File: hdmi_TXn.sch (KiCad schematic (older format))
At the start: 21 parts

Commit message: Fix issues due to different KiCad version
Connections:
- wire segments 106 -> 96
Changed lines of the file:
@@
 U 1 1 57C07751
 P 10600 4950
+AR Path="/57C07751" Ref="R$TXn$3"  Part="1"
+AR Path="/57C01383/57C07751" Ref="R$TXn$3"  Part="1"
 F 0 "R$TXn$3" V 10700 4950 50  0000 C CNN
 F 1 "R" V 10607 4951 50  0000 C CNN
@@
 U 1 1 57C07753
 P 3900 4400
+AR Path="/57C07753" Ref="R$TXn$1"  Part="1"
+AR Path="/57C01383/57C07753" Ref="R$TXn$1"  Part="1"
 F 0 "R$TXn$1" V 3800 4400 50  0000 C CNN
 F 1 "R" V 3907 4401 50  0000 C CNN
@@
 U 1 1 57C07755
 P 4000 4400
+AR Path="/57C07755" Ref="R$TXn$2"  Part="1"
+AR Path="/57C01383/57C07755" Ref="R$TXn$2"  Part="1"
 F 0 "R$TXn$2" V 4080 4400 50  0000 C CNN
 F 1 "R" V 4007 4401 50  0000 C CNN
@@
 	11750 4850 11600 4850
 Wire Wire Line
-	11600 4850 11600 5150
-Wire Wire Line
-	11600 5150 11600 5450
-Wire Wire Line
-	11600 5450 11600 5750
-Wire Wire Line
-	11600 5750 11600 6350
-Wire Wire Line
-	11600 6350 11600 6900
+	11600 4850 11600 6900
 Wire Wire Line
 	11750 5150 11600 5150
@@
 	6400 5800 6750 5800
 Wire Wire Line
-	8150 6600 8550 6600
-Wire Wire Line
-	8550 6600 9000 6600
+	8150 6600 9000 6600
 Wire Wire Line
 	8150 6400 9000 6400
 Wire Wire Line
-	7400 3750 7450 3750
-Wire Wire Line
-	7450 3750 7500 3750
+	7400 3750 7500 3750
 Wire Wire Line
 	7450 3750 7450 3600
@@
 Connection ~ 11600 6350
 Wire Wire Line
-	9800 5950 10600 5950
-Wire Wire Line
-	10600 5950 11750 5950
+	9800 5950 11750 5950
 Wire Wire Line
 	10600 5950 10600 5650
 Wire Wire Line
-	10600 5200 10600 5250
-Wire Wire Line
-	10600 4450 10600 4700
+	10600 5100 10600 5250
+Wire Wire Line
+	10600 4450 10600 4800
 Connection ~ 10600 5950
 Wire Wire Line
@@
 	5400 4800 6200 4800
 Wire Wire Line
-	4000 4100 4000 4150
+	4000 4100 4000 4250
 $Comp
 L VCC3V3 #PWR3
@@
 $EndComp
 Wire Wire Line
-	3900 4100 3950 4100
-Wire Wire Line
-	3950 4100 4000 4100
+	3900 4100 4000 4100
 Text Label 3800 5900 2    60   ~ 0
 HDMIP_$TXn$_SCL
@@
 U 1 1 57C07769
 P 3900 5600
+AR Path="/57C07769" Ref="R$TXn$4"  Part="1"
+AR Path="/57C01383/57C07769" Ref="R$TXn$4"  Part="1"
 F 0 "R$TXn$4" V 3800 5600 50  0000 C CNN
 F 1 "R" V 3907 5601 50  0000 C CNN
@@
 U 1 1 57B7FCE7
 P 4000 5600
+AR Path="/57B7FCE7" Ref="R$TXn$5"  Part="1"
+AR Path="/57C01383/57B7FCE7" Ref="R$TXn$5"  Part="1"
 F 0 "R$TXn$5" V 4080 5600 50  0000 C CNN
 F 1 "R" V 4007 5601 50  0000 C CNN
@@
 U 1 1 57C0776D
 P 6500 6900
+AR Path="/57C0776D" Ref="R$TXn$6"  Part="1"
+AR Path="/57C01383/57C0776D" Ref="R$TXn$6"  Part="1"
 F 0 "R$TXn$6" V 6580 6900 50  0000 C CNN
 F 1 "R" V 6507 6901 50  0000 C CNN
@@
 $EndComp
 Wire Wire Line
-	6500 6300 6500 6650
+	6500 6300 6500 6750
 $Comp
 L GND #PWR9
@@
 HDMI_$TXn$_SDA
 Wire Wire Line
-	3800 4700 3900 4700
-Wire Wire Line
-	3900 4700 3900 4650
-Wire Wire Line
-	3800 4800 4000 4800
-Wire Wire Line
-	4000 4800 4000 4650
+	3900 4700 3800 4700
+Wire Wire Line
+	3900 4550 3900 4700
+Wire Wire Line
+	4000 4800 3800 4800
+Wire Wire Line
+	4000 4550 4000 4800
 Text Label 5700 6400 0    60   ~ 0
 HDMI_$TXn$_DDET
@@
 ~HDMI_$TXn$_OE
 Wire Wire Line
-	3800 5900 3900 5900
-Wire Wire Line
-	3900 5900 3900 5850
-Wire Wire Line
-	3800 6000 4000 6000
-Wire Wire Line
-	4000 6000 4000 5850
-Wire Wire Line
-	3900 5300 3900 5350
-Wire Wire Line
-	3900 5300 3950 5300
-Wire Wire Line
-	3950 5300 4000 5300
-Wire Wire Line
-	4000 5300 4000 5350
+	3900 5900 3800 5900
+Wire Wire Line
+	3900 5750 3900 5900
+Wire Wire Line
+	4000 6000 3800 6000
+Wire Wire Line
+	4000 5750 4000 6000
+Wire Wire Line
+	3900 5300 3900 5450
+Wire Wire Line
+	3900 5300 4000 5300
+Wire Wire Line
+	4000 5300 4000 5450
 Wire Wire Line
 	3950 5300 3950 5150
 Connection ~ 3950 5300
 Wire Wire Line
-	3900 4100 3900 4150
+	3900 4100 3900 4250
 Wire Wire Line
 	3950 4050 3950 4100
@@
 U 1 1 57C07777
 P 8500 3850
+AR Path="/57C07777" Ref="C$TXn$2"  Part="1"
+AR Path="/57C01383/57C07777" Ref="C$TXn$2"  Part="1"
 F 0 "C$TXn$2" H 8300 3750 30  0000 L CNN
 F 1 "100n" H 8300 3850 30  0000 L CNN
@@
 U 1 1 57C07779
 P 8300 3850
+AR Path="/57C07779" Ref="C$TXn$1"  Part="1"
+AR Path="/57C01383/57C07779" Ref="C$TXn$1"  Part="1"
 F 0 "C$TXn$1" H 8350 3750 30  0000 L CNN
 F 1 "100n" H 8400 3850 30  0000 L CNN
@@
 $EndComp
 Wire Wire Line
-	8300 3600 8400 3600
-Wire Wire Line
-	8400 3600 8500 3600
-Wire Wire Line
-	8300 3600 8300 3650
-Wire Wire Line
-	8500 3600 8500 3650
+	8300 3600 8500 3600
+Wire Wire Line
+	8300 3600 8300 3700
+Wire Wire Line
+	8500 3600 8500 3700
 Connection ~ 8400 3600
 Wire Wire Line
-	8300 4050 8300 4100
-Wire Wire Line
-	8300 4100 8400 4100
-Wire Wire Line
-	8400 4100 8500 4100
-Wire Wire Line
-	8500 4100 8500 4050
+	8300 4000 8300 4100
+Wire Wire Line
+	8300 4100 8500 4100
+Wire Wire Line
+	8500 4100 8500 4000
 $Comp
 L GND #PWR4
@@
 Text HLabel 9800 5950 0    60   Input ~ 0
 HDMI_$TXn$_CEC
+Wire Wire Line
+	6500 7050 6500 7150
 $EndSCHEMATC

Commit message: Fix caps issues in templates
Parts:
- C$TXn$11: symbol Csmall -> C_Small
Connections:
- wire segments 96 -> 107
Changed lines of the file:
@@
 LIBS:hdmi2usb
 LIBS:HDMI2USB-cache
-LIBS:HDMI2USB-pcie-artix7-cache
 EELAYER 25 0
 EELAYER END
 $Descr A3 16535 11693
 encoding utf-8
-Sheet 7 14
+Sheet 1 1
 Title ""
 Date ""
@@
 	11750 4850 11600 4850
 Wire Wire Line
-	11600 4850 11600 6900
+	11600 4850 11600 5150
+Wire Wire Line
+	11600 5150 11600 5450
+Wire Wire Line
+	11600 5450 11600 5750
+Wire Wire Line
+	11600 5750 11600 6350
+Wire Wire Line
+	11600 6350 11600 6900
 Wire Wire Line
 	11750 5150 11600 5150
@@
 	6400 5800 6750 5800
 Wire Wire Line
-	8150 6600 9000 6600
+	8150 6600 8550 6600
+Wire Wire Line
+	8550 6600 9000 6600
 Wire Wire Line
 	8150 6400 9000 6400
 Wire Wire Line
-	7400 3750 7500 3750
+	7400 3750 7450 3750
+Wire Wire Line
+	7450 3750 7500 3750
 Wire Wire Line
 	7450 3750 7450 3600
@@
 Connection ~ 11600 6350
 Wire Wire Line
-	9800 5950 11750 5950
+	9800 5950 10600 5950
+Wire Wire Line
+	10600 5950 11750 5950
 Wire Wire Line
 	10600 5950 10600 5650
@@
 $EndComp
 Wire Wire Line
-	3900 4100 4000 4100
+	3900 4100 3950 4100
+Wire Wire Line
+	3950 4100 4000 4100
 Text Label 3800 5900 2    60   ~ 0
 HDMIP_$TXn$_SCL
@@
 	3900 5300 3900 5450
 Wire Wire Line
-	3900 5300 4000 5300
+	3900 5300 3950 5300
+Wire Wire Line
+	3950 5300 4000 5300
 Wire Wire Line
 	4000 5300 4000 5450
@@
 $EndComp
 $Comp
-L Csmall C$TXn$11
+L C_Small C$TXn$11
 U 1 1 57C07774
 P 8550 6850
@@
 $EndComp
 Wire Wire Line
-	8300 3600 8500 3600
+	8300 3600 8400 3600
+Wire Wire Line
+	8400 3600 8500 3600
 Wire Wire Line
 	8300 3600 8300 3700
@@
 	8300 4000 8300 4100
 Wire Wire Line
-	8300 4100 8500 4100
+	8300 4100 8400 4100
+Wire Wire Line
+	8400 4100 8500 4100
 Wire Wire Line
 	8500 4100 8500 4000

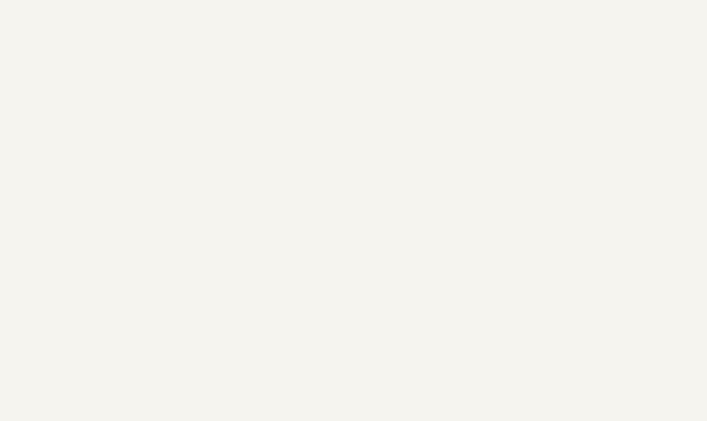
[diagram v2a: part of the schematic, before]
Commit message: Adding warning text.
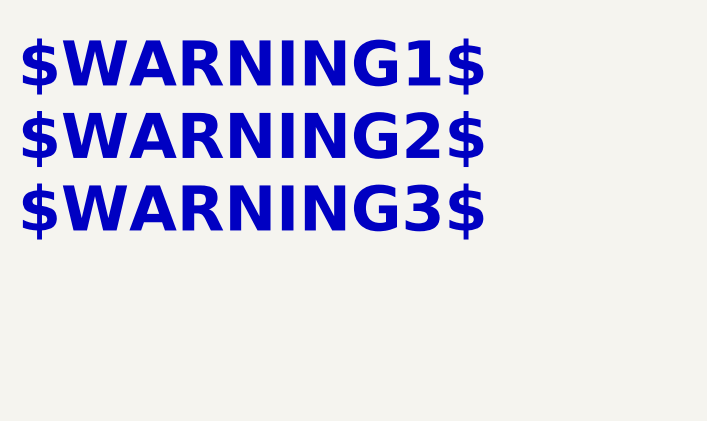
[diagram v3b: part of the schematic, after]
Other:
- note added: "$WARNING1$\n$WARNING2$\n$WARNING3$"
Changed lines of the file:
@@
 Wire Wire Line
 	6500 7050 6500 7150
+Text Notes 930  1790 0    197  ~ 39
+$WARNING1$\n$WARNING2$\n$WARNING3$
 $EndSCHEMATC

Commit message: Add CEC to HDMI headers.
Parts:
- removed P$TXn$1: CONN_5, symbol CONN_5
- added P$TXn$1: CONN_01X06, symbol CONN_01X06
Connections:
- wire segments 107 -> 97
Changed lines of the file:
@@
 LIBS:hdmi2usb
 LIBS:HDMI2USB-cache
+LIBS:hdmi_TXn-cache
 EELAYER 25 0
 EELAYER END
@@
 	11750 4850 11600 4850
 Wire Wire Line
-	11600 4850 11600 5150
-Wire Wire Line
-	11600 5150 11600 5450
-Wire Wire Line
-	11600 5450 11600 5750
-Wire Wire Line
-	11600 5750 11600 6350
-Wire Wire Line
-	11600 6350 11600 6900
+	11600 4850 11600 6900
 Wire Wire Line
 	11750 5150 11600 5150
@@
 	6400 5800 6750 5800
 Wire Wire Line
-	8150 6600 8550 6600
-Wire Wire Line
-	8550 6600 9000 6600
+	8150 6600 9000 6600
 Wire Wire Line
 	8150 6400 9000 6400
 Wire Wire Line
-	7400 3750 7450 3750
-Wire Wire Line
-	7450 3750 7500 3750
+	7400 3750 7500 3750
 Wire Wire Line
 	7450 3750 7450 3600
@@
 Connection ~ 11600 6350
 Wire Wire Line
-	9800 5950 10600 5950
-Wire Wire Line
-	10600 5950 11750 5950
+	9800 5950 11750 5950
 Wire Wire Line
 	10600 5950 10600 5650
@@
 $EndComp
 Wire Wire Line
-	3900 4100 3950 4100
-Wire Wire Line
-	3950 4100 4000 4100
+	3900 4100 4000 4100
 Text Label 3800 5900 2    60   ~ 0
 HDMIP_$TXn$_SCL
@@
 	3900 5300 3900 5450
 Wire Wire Line
-	3900 5300 3950 5300
-Wire Wire Line
-	3950 5300 4000 5300
+	3900 5300 4000 5300
 Wire Wire Line
 	4000 5300 4000 5450
@@
 $EndComp
 Wire Wire Line
-	8300 3600 8400 3600
-Wire Wire Line
-	8400 3600 8500 3600
+	8300 3600 8500 3600
 Wire Wire Line
 	8300 3600 8300 3700
@@
 	8300 4000 8300 4100
 Wire Wire Line
-	8300 4100 8400 4100
-Wire Wire Line
-	8400 4100 8500 4100
+	8300 4100 8500 4100
 Wire Wire Line
 	8500 4100 8500 4000
@@
 Text Label 9000 6400 2    60   ~ 0
 HDMI_$TXn$_HIZ_EN
-$Comp
-L CONN_5 P$TXn$1
-U 1 1 57BC59B8
-P 4200 6900
-F 0 "P$TXn$1" H 4200 7200 50  0000 C CNN
-F 1 "CONN_5" V 4250 6900 40  0000 C CNN
-F 2 "" H 4200 6900 60  0000 C CNN
-F 3 "" H 4200 6900 60  0000 C CNN
-	1    4200 6900
-	1    0    0    -1
-$EndComp
 Text Label 3050 6900 0    60   ~ 0
 HDMI_$TXn$_HPD
@@
 L VCC3V3 #PWR7
 U 1 1 57BC61BF
-P 3300 7000
-F 0 "#PWR7" H 3300 6850 60  0001 C CNN
-F 1 "VCC3V3" V 3300 7300 60  0000 C CNN
-F 2 "" H 3300 7000 60  0000 C CNN
-F 3 "" H 3300 7000 60  0000 C CNN
-	1    3300 7000
-	0    -1   -1   0
+P 3735 7140
+F 0 "#PWR7" H 3735 6990 60  0001 C CNN
+F 1 "VCC3V3" H 3950 7195 60  0000 C CNN
+F 2 "" H 3735 7140 60  0000 C CNN
+F 3 "" H 3735 7140 60  0000 C CNN
+	1    3735 7140
+	-1   0    0    1
 $EndComp
 $Comp
 L GND #PWR8
 U 1 1 57C07784
-P 3700 7150
-F 0 "#PWR8" H 3700 6900 60  0001 C CNN
-F 1 "GND" H 3700 7000 60  0000 C CNN
-F 2 "" H 3700 7150 60  0000 C CNN
-F 3 "" H 3700 7150 60  0000 C CNN
-	1    3700 7150
-	1    0    0    -1
-$EndComp
-Wire Wire Line
-	3800 7100 3700 7100
-Wire Wire Line
-	3700 7100 3700 7150
-Wire Wire Line
-	3300 7000 3800 7000
+P 3625 7000
+F 0 "#PWR8" H 3625 6750 60  0001 C CNN
+F 1 "GND" H 3625 6850 60  0000 C CNN
+F 2 "" H 3625 7000 60  0000 C CNN
+F 3 "" H 3625 7000 60  0000 C CNN
+	1    3625 7000
+	0    1    1    0
+$EndComp
 Wire Wire Line
 	3800 6900 3050 6900
@@
 Text Notes 930  1790 0    197  ~ 39
 $WARNING1$\n$WARNING2$\n$WARNING3$
+$Comp
+L CONN_01X06 P$TXn$1
+U 1 1 57D6599C
+P 4000 6850
+F 0 "P$TXn$1" H 4078 6891 50  0000 L CNN
+F 1 "CONN_01X06" H 4078 6800 50  0000 L CNN
+F 2 "" H 4000 6850 50  0000 C CNN
+F 3 "" H 4000 6850 50  0000 C CNN
+	1    4000 6850
+	1    0    0    -1
+$EndComp
+Wire Wire Line
+	3800 7000 3625 7000
+Wire Wire Line
+	3735 7140 3735 7100
+Wire Wire Line
+	3735 7100 3800 7100
+Wire Wire Line
+	3800 6600 3050 6600
+Text Label 3050 6600 0    60   ~ 0
+HDMI_$TXn$_CEC
 $EndSCHEMATC

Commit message: Adding more to the debug header (making it PMOD compatible).
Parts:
- removed P$TXn$1: CONN_01X06, symbol CONN_01X06
- added P$TXn$1: CONN_02X06, symbol CONN_02X06
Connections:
- wire segments 97 -> 122
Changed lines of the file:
@@
 	11750 4850 11600 4850
 Wire Wire Line
-	11600 4850 11600 6900
+	11600 4850 11600 5150
+Wire Wire Line
+	11600 5150 11600 5450
+Wire Wire Line
+	11600 5450 11600 5750
+Wire Wire Line
+	11600 5750 11600 6350
+Wire Wire Line
+	11600 6350 11600 6900
 Wire Wire Line
 	11750 5150 11600 5150
@@
 	6400 5800 6750 5800
 Wire Wire Line
-	8150 6600 9000 6600
+	8150 6600 8550 6600
+Wire Wire Line
+	8550 6600 9000 6600
 Wire Wire Line
 	8150 6400 9000 6400
 Wire Wire Line
-	7400 3750 7500 3750
+	7400 3750 7450 3750
+Wire Wire Line
+	7450 3750 7500 3750
 Wire Wire Line
 	7450 3750 7450 3600
@@
 Connection ~ 11600 6350
 Wire Wire Line
-	9800 5950 11750 5950
+	9800 5950 10600 5950
+Wire Wire Line
+	10600 5950 11750 5950
 Wire Wire Line
 	10600 5950 10600 5650
@@
 $EndComp
 Wire Wire Line
-	3900 4100 4000 4100
+	3900 4100 3950 4100
+Wire Wire Line
+	3950 4100 4000 4100
 Text Label 3800 5900 2    60   ~ 0
 HDMIP_$TXn$_SCL
@@
 	3900 5300 3900 5450
 Wire Wire Line
-	3900 5300 4000 5300
+	3900 5300 3950 5300
+Wire Wire Line
+	3950 5300 4000 5300
 Wire Wire Line
 	4000 5300 4000 5450
@@
 $EndComp
 Wire Wire Line
-	8300 3600 8500 3600
+	8300 3600 8400 3600
+Wire Wire Line
+	8400 3600 8500 3600
 Wire Wire Line
 	8300 3600 8300 3700
@@
 	8300 4000 8300 4100
 Wire Wire Line
-	8300 4100 8500 4100
+	8300 4100 8400 4100
+Wire Wire Line
+	8400 4100 8500 4100
 Wire Wire Line
 	8500 4100 8500 4000
@@
 Text Label 9000 6400 2    60   ~ 0
 HDMI_$TXn$_HIZ_EN
-Text Label 3050 6900 0    60   ~ 0
+Text Label 2415 6870 0    60   ~ 0
 HDMI_$TXn$_HPD
-Text Label 3050 6700 0    60   ~ 0
+Text Label 2415 6670 0    60   ~ 0
 HDMI_$TXn$_SCL
-Text Label 3050 6800 0    60   ~ 0
+Text Label 2415 6770 0    60   ~ 0
 HDMI_$TXn$_SDA
 $Comp
 L VCC3V3 #PWR7
 U 1 1 57BC61BF
-P 3735 7140
-F 0 "#PWR7" H 3735 6990 60  0001 C CNN
-F 1 "VCC3V3" H 3950 7195 60  0000 C CNN
-F 2 "" H 3735 7140 60  0000 C CNN
-F 3 "" H 3735 7140 60  0000 C CNN
-	1    3735 7140
+P 3100 7110
+F 0 "#PWR7" H 3100 6960 60  0001 C CNN
+F 1 "VCC3V3" H 3315 7165 60  0000 C CNN
+F 2 "" H 3100 7110 60  0000 C CNN
+F 3 "" H 3100 7110 60  0000 C CNN
+	1    3100 7110
 	-1   0    0    1
 $EndComp
@@
 L GND #PWR8
 U 1 1 57C07784
-P 3625 7000
-F 0 "#PWR8" H 3625 6750 60  0001 C CNN
-F 1 "GND" H 3625 6850 60  0000 C CNN
-F 2 "" H 3625 7000 60  0000 C CNN
-F 3 "" H 3625 7000 60  0000 C CNN
-	1    3625 7000
-	0    1    1    0
-$EndComp
-Wire Wire Line
-	3800 6900 3050 6900
-Wire Wire Line
-	3800 6800 3050 6800
-Wire Wire Line
-	3800 6700 3050 6700
+P 2610 6970
+F 0 "#PWR8" H 2610 6720 60  0001 C CNN
+F 1 "GND" H 2610 6820 60  0000 C CNN
+F 2 "" H 2610 6970 60  0000 C CNN
+F 3 "" H 2610 6970 60  0000 C CNN
+	1    2610 6970
+	0    1    1    0
+$EndComp
+Wire Wire Line
+	3165 6870 2415 6870
+Wire Wire Line
+	3165 6770 2415 6770
+Wire Wire Line
+	3165 6670 2415 6670
 Text HLabel 5850 4100 0    60   Input ~ 0
 ~HDMI_$TXn$_OE
@@
 Text Notes 930  1790 0    197  ~ 39
 $WARNING1$\n$WARNING2$\n$WARNING3$
-$Comp
-L CONN_01X06 P$TXn$1
-U 1 1 57D6599C
-P 4000 6850
-F 0 "P$TXn$1" H 4078 6891 50  0000 L CNN
-F 1 "CONN_01X06" H 4078 6800 50  0000 L CNN
-F 2 "" H 4000 6850 50  0000 C CNN
-F 3 "" H 4000 6850 50  0000 C CNN
-	1    4000 6850
-	1    0    0    -1
-$EndComp
-Wire Wire Line
-	3800 7000 3625 7000
-Wire Wire Line
-	3735 7140 3735 7100
-Wire Wire Line
-	3735 7100 3800 7100
-Wire Wire Line
-	3800 6600 3050 6600
-Text Label 3050 6600 0    60   ~ 0
+Wire Wire Line
+	3165 6970 2680 6970
+Wire Wire Line
+	2680 6970 2610 6970
+Wire Wire Line
+	3100 7110 3100 7070
+Wire Wire Line
+	3100 7070 3145 7070
+Wire Wire Line
+	3145 7070 3165 7070
+Wire Wire Line
+	3165 6570 2415 6570
+Text Label 2415 6570 0    60   ~ 0
 HDMI_$TXn$_CEC
+$Comp
+L CONN_02X06 P$TXn$1
+U 1 1 57D65C54
+P 3415 6820
+F 0 "P$TXn$1" H 3415 7285 50  0000 C CNN
+F 1 "CONN_02X06" H 3415 7194 50  0000 C CNN
+F 2 "" H 3415 5620 50  0000 C CNN
+F 3 "" H 3415 5620 50  0000 C CNN
+	1    3415 6820
+	1    0    0    -1
+$EndComp
+Wire Wire Line
+	3145 7070 3145 7205
+Wire Wire Line
+	3145 7205 3700 7205
+Wire Wire Line
+	3700 7205 3700 7070
+Wire Wire Line
+	3700 7070 3665 7070
+Connection ~ 3145 7070
+Wire Wire Line
+	2680 6970 2680 7270
+Wire Wire Line
+	2680 7270 3755 7270
+Wire Wire Line
+	3755 7270 3755 6970
+Wire Wire Line
+	3755 6970 3665 6970
+Connection ~ 2680 6970
+Text Label 4535 6865 2    60   ~ 0
+HDMI_$TXn$_DDET
+Text Label 4535 6665 2    60   ~ 0
+HDMI_$TXn$_EQ1
+Text Label 4535 6765 2    60   ~ 0
+HDMI_$TXn$_DDC_EN
+Wire Wire Line
+	4535 6865 3665 6870
+Wire Wire Line
+	4535 6765 3665 6770
+Wire Wire Line
+	4535 6665 3665 6670
+Wire Wire Line
+	4535 6565 3665 6570
+Text Label 4535 6565 2    60   ~ 0
+HDMI_$TXn$_EQ0
 $EndSCHEMATC

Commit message: Changes to the HDMI template.
 * Change the component numbering to better match the Axiom schematic.
 * Added footprints to almost all components.
 * Added values to things which needed values.
 * Added `desc` and `manf#` to most components.
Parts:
- removed C$TXn$10, C$TXn$9: 100n, symbol Csmall
- added C$TXn$3, C$TXn$4: 100n, Capacitors_SMD:C_0402, symbol Csmall
- C$TXn$1: renamed from C$TXn$3; footprint (none) -> Capacitors_SMD:C_0402; desc (none) -> 0402, X7R, 0.10µF, 16Vdc; manf# (none) -> GRM155R71C104KA88D
- C$TXn$13: renamed from C$TXn$11; footprint (none) -> Capacitors_SMD:C_0402; desc (none) -> 0402, X7R, 10000pF, 25Vdc; manf# (none) -> GRM155R71E103KA01D
- C$TXn$16: renamed from C$TXn$1; footprint (none) -> Capacitors_SMD:C_0402; desc (none) -> 0402, X7R, 0.10µF, 16Vdc; manf# (none) -> GRM155R71C104KA88D
- C$TXn$17: renamed from C$TXn$2; footprint (none) -> Capacitors_SMD:C_0402; desc (none) -> 0402, X7R, 0.10µF, 16Vdc; manf# (none) -> GRM155R71C104KA88D
- C$TXn$2: renamed from C$TXn$4; footprint (none) -> Capacitors_SMD:C_0402; desc (none) -> 0402, X7R, 0.10µF, 16Vdc; manf# (none) -> GRM155R71C104KA88D
- C$TXn$5, C$TXn$6, C$TXn$7, C$TXn$8: footprint (none) -> Capacitors_SMD:C_0402; desc (none) -> 0402, X7R, 0.10µF, 16Vdc; manf# (none) -> GRM155R71C104KA88D
- J$TXn$1: manf# (none) -> 10029449-001RLF
- P$TXn$1: footprint (none) -> Pin_Headers:Pin_Header_Straight_2x06
- R$TXn$1: renamed from R$TXn$2; value R -> 2k2; footprint (none) -> Resistors_SMD:R_0402; desc (none) -> 0402, 2k2 Ohm, 1%; manf# (none) -> RC0402FR-072K2L
- R$TXn$2: renamed from R$TXn$1; value R -> 2k2; footprint (none) -> Resistors_SMD:R_0402; desc (none) -> 0402, 2k2 Ohm, 1%; manf# (none) -> RC0402FR-072K2L
- R$TXn$3: renamed from R$TXn$6; value R -> 12k4; footprint (none) -> Resistors_SMD:R_0402; desc (none) -> 0402, 12k4 Ohm, 1%; manf# (none) -> ERJ-2RKF1242X
- R$TXn$4, R$TXn$5: value R -> 2k2; footprint (none) -> Resistors_SMD:R_0402; desc (none) -> 0402, 2k2 Ohm, 1%; manf# (none) -> RC0402FR-072K2L
- R$TXn$8: renamed from R$TXn$3; footprint (none) -> Resistors_SMD:R_0402; desc (none) -> 0402, 2k2 Ohm, 1%; manf# (none) -> RC0402FR-072K2L
- U$TXn$1: footprint (none) -> Housings_DFN_QFN:QFN-32-1EP_5x5mm_Pitch0.5mm; digikey# (none) -> 568-11580-6-ND; manf# (none) -> PTN3363BSMP
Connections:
- wire segments 122 -> 109
